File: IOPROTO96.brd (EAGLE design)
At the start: 38.1 x 39.4 mm, 4 parts

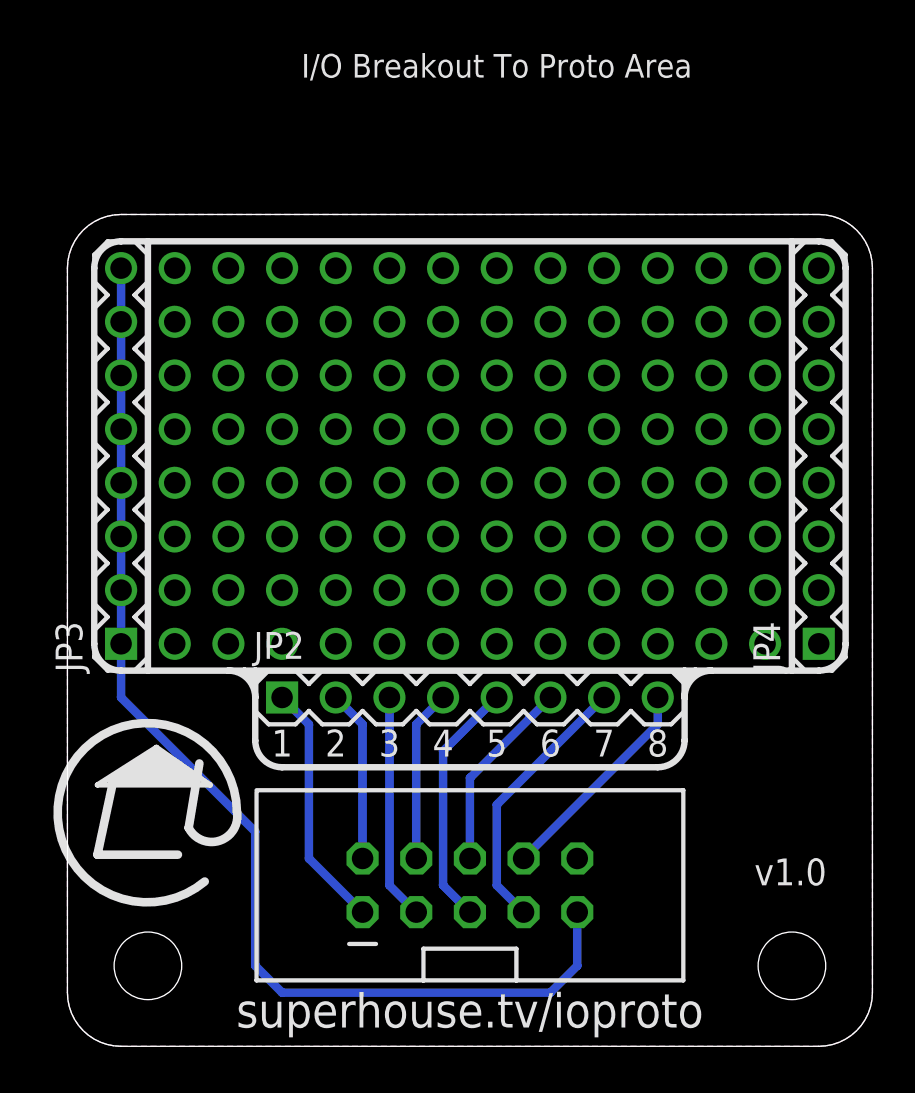
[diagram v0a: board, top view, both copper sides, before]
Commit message: Updated silkscreen for v2.0 release
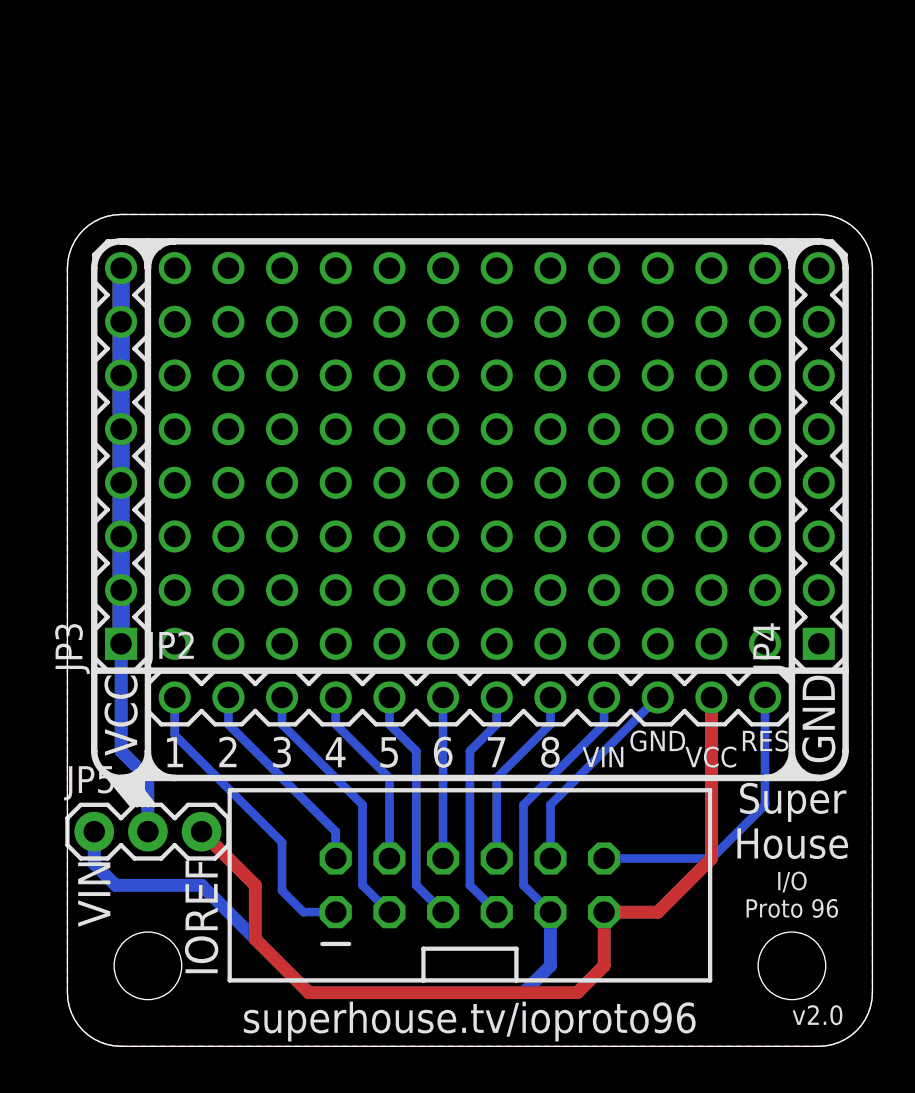
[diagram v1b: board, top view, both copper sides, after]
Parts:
- added JP5: (no value), freetronics-jon:1X03
- JP1: value M05X2SHD -> M06X2; device freetronics-original:2X5-SHROUDED -> freetronics-jon:2X6-SHROUDED
- JP2: value (none) -> M12PTH; device freetronics-master-v1:1X08 -> freetronics-original:1X12
- moved JP1 6.48 mm to (12.7, 6.35)
- moved JP2 5.08 mm to (5.08, 16.5)
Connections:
- net N$11 renamed D5
- net N$12 renamed D3
- net N$13 renamed D1
- net N$14 renamed D7
- net N$27 renamed D8
- net N$28 renamed D6
- net N$29 renamed D4
- net N$30 renamed D2
- removed net VCC: JP1.9, JP3.1, JP3.2, JP3.3, JP3.4, JP3.5, JP3.6, JP3.7, JP3.8
- new net IOREF: JP1.11, JP2.11, JP5.3
- new net RESET: JP1.12, JP2.12
- new net V+: JP3.1, JP3.2, JP3.3, JP3.4, JP3.5, JP3.6, JP3.7, JP3.8, JP5.2
- new net VIN: JP1.9, JP2.9, JP5.1
- net GND: now also JP2.10
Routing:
- net VCC: track 54.5 -> 0.00 mm
- net VIN: track 0.00 -> 41.0 mm
- net IOREF: track 0.00 -> 40.5 mm
- net V+: track 0.00 -> 27.2 mm
- net RESET: track 0.00 -> 13.8 mm
- net GND: track 0.00 -> 9.72 mm
- net D1: track 11.7 -> 14.2 mm
- net D8: track 10.3 -> 8.67 mm
- net D3: track 10.7 -> 12.3 mm
- net D6: track 9.20 -> 7.62 mm
- net D2: track 8.15 -> 9.72 mm
- net D7: track 12.8 -> 11.2 mm
- net D4: track 8.15 -> 8.67 mm
- net D5: track 11.7 -> 11.2 mm
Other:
- board text added: "(c) 2017 SuperHouse"
- board text added: "I/O Proto 96"
- board text added: "IOREF"
- board text added: "RES"
- board text added: "RESET"
- board text added: "SKU: IOPROTO96"
- board text added: "Super House"
- board text added: "VIN"
- board text added: "superhouse.tv/ioproto96"
- board text added: "v2.0"
- board text removed: "(c) 2017 SuperHouse Pty Ltd"
- board text removed: "I/O Breakout To Proto Area"
- board text removed: "Licensed under the TAPR"
- board text removed: "Open Hardware License"
- board text removed: "SKU: IOTERM"
- board text removed: "superhouse.tv/ioproto"
- board text removed: "v1.0"
- board text removed: "www.tapr.org/OHL"

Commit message: Final routing and DRC for release v2.0
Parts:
- moved JP5 4.58 mm to (3.81, 6.35), turned to 90 degrees
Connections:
- net D1 renamed IO1
- net D2 renamed IO2
- net D3 renamed IO3
- net D4 renamed IO4
- net D5 renamed IO5
- net D6 renamed IO6
- net D7 renamed IO7
- net D8 renamed IO8
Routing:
- net GND: track 9.72 -> 0.00 mm
- net VIN: track 41.0 -> 36.0 mm
- net IOREF: track 40.5 -> 44.3 mm
- net V+: track 27.2 -> 30.3 mm
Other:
- board text added: "IO REF"

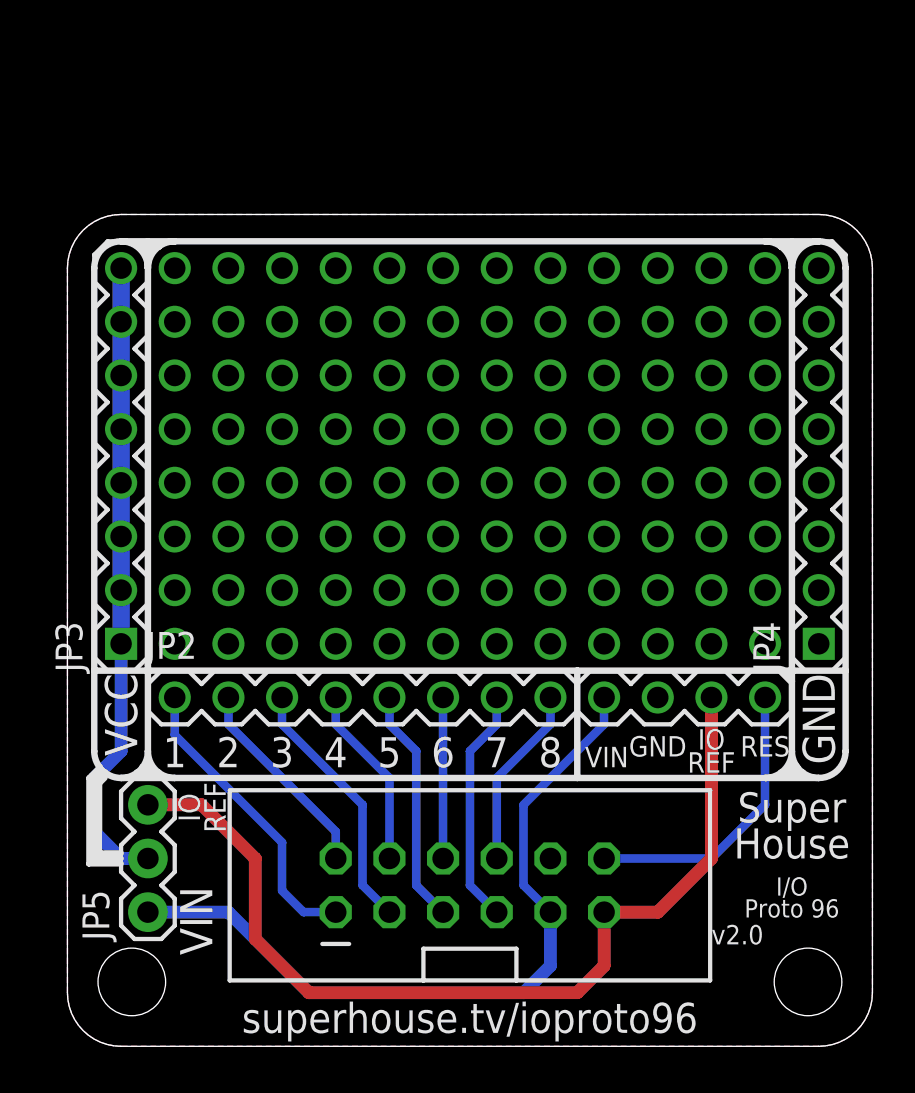
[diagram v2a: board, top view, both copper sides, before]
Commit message: Part replacement using SuperHouse libraries
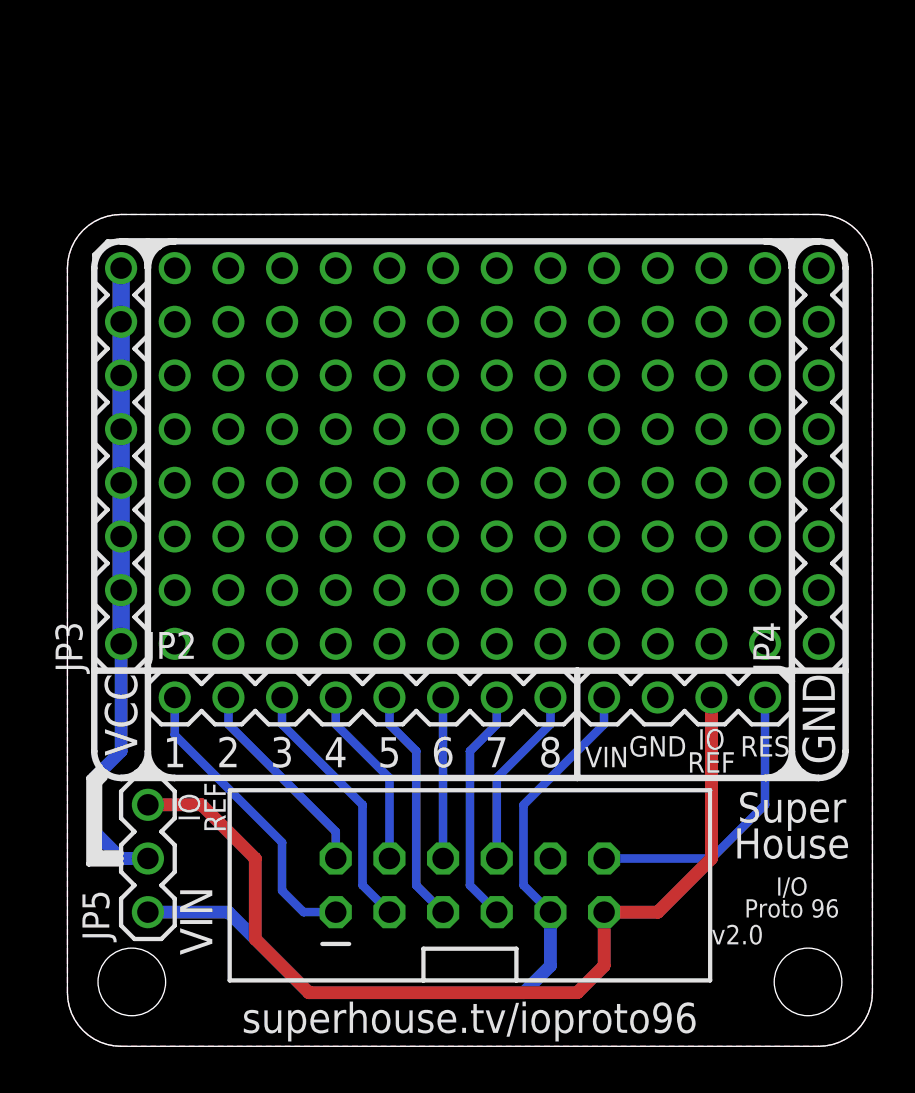
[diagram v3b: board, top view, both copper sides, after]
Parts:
- JP1: value M06X2 -> M06X2-SHROUDED; device freetronics-jon:2X6-SHROUDED -> SuperHouse-Connectors:2X6-SHROUDED
- JP2: value M12PTH -> M12-PLAIN; device freetronics-original:1X12 -> SuperHouse-Connectors:1X12
- JP3, JP4: value (none) -> M08-PLAIN; device freetronics-master-v1:1X08 -> SuperHouse-Connectors:1X08
- JP5: device freetronics-jon:1X03 -> SuperHouse-Connectors:1X03-P
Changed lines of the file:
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@@
 <?xml version="1.0" encoding="utf-8"?>
 <!DOCTYPE eagle SYSTEM "eagle.dtd">
-<eagle version="6.5.0">
+<eagle version="9.4.2">
 <drawing>
 <settings>
 <setting alwaysvectorfont="yes"/>
+<setting keepoldvectorfont="yes"/>
 <setting verticaltext="up"/>
 </settings>
@@
 <layer number="60" name="bCarbon" color="7" fill="1" visible="no" active="no"/>
 <layer number="61" name="pt_docu" color="7" fill="0" visible="no" active="no"/>
-<layer number="90" name="Modules" color="7" fill="1" visible="yes" active="yes"/>
+<layer number="88" name="SimResults" color="9" fill="1" visible="no" active="no"/>
+<layer number="89" name="SimProbes" color="9" fill="1" visible="no" active="no"/>
+<layer number="90" name="Modules" color="7" fill="1" visible="no" active="no"/>
 <layer number="91" name="Nets" color="2" fill="1" visible="no" active="no"/>
 <layer number="92" name="Busses" color="1" fill="1" visible="no" active="no"/>
@@
 <layer number="131" name="tAdjust" color="7" fill="1" visible="yes" active="yes"/>
 <layer number="132" name="bAdjust" color="7" fill="1" visible="yes" active="yes"/>
+<layer number="133" name="bottom_silk" color="7" fill="1" visible="yes" active="yes"/>
+<layer number="134" name="silk_top" color="7" fill="1" visible="no" active="no"/>
+<layer number="135" name="silk_bottom" color="7" fill="1" visible="no" active="no"/>
+<layer number="136" name="silktop" color="7" fill="1" visible="yes" active="yes"/>
+<layer number="137" name="silkbottom" color="7" fill="1" visible="yes" active="yes"/>
+<layer number="138" name="GND@2" color="7" fill="1" visible="yes" active="yes"/>
+<layer number="139" name="mtKeepout" color="7" fill="1" visible="yes" active="yes"/>
+<layer number="140" name="mbKeepout" color="7" fill="1" visible="yes" active="yes"/>
+<layer number="141" name="mtRestrict" color="7" fill="1" visible="yes" active="yes"/>
+<layer number="142" name="mbRestrict" color="7" fill="1" visible="yes" active="yes"/>
+<layer number="143" name="mvRestrict" color="7" fill="1" visible="yes" active="yes"/>
 <layer number="144" name="Drill_legend" color="7" fill="1" visible="yes" active="yes"/>
+<layer number="145" name="DrillLegend_01-16" color="7" fill="1" visible="yes" active="yes"/>
 <layer number="146" name="p_Milling" color="3" fill="9" visible="no" active="yes"/>
 <layer number="147" name="COVER" color="14" fill="1" visible="no" active="yes"/>
+<layer number="148" name="mDocument" color="7" fill="1" visible="yes" active="yes"/>
+<layer number="149" name="mReference" color="7" fill="1" visible="yes" active="yes"/>
 <layer number="150" name="Notes" color="7" fill="1" visible="yes" active="yes"/>
 <layer number="151" name="HeatSink" color="7" fill="1" visible="yes" active="yes"/>
@@
 <layer number="154" name="FabDoc2" color="2" fill="1" visible="no" active="no"/>
 <layer number="155" name="FabDoc3" color="7" fill="15" visible="no" active="no"/>
+<layer number="166" name="AntennaArea" color="7" fill="1" visible="yes" active="yes"/>
+<layer number="168" name="4mmHeightArea" color="7" fill="1" visible="yes" active="yes"/>
 <layer number="190" name="Comments" color="12" fill="1" visible="no" active="yes"/>
+<layer number="191" name="mNets" color="7" fill="1" visible="yes" active="yes"/>
+<layer number="192" name="mBusses" color="7" fill="1" visible="yes" active="yes"/>
+<layer number="193" name="mPins" color="7" fill="1" visible="yes" active="yes"/>
+<layer number="194" name="mSymbols" color="7" fill="1" visible="yes" active="yes"/>
+<layer number="195" name="mNames" color="7" fill="1" visible="yes" active="yes"/>
+<layer number="196" name="mValues" color="7" fill="1" visible="yes" active="yes"/>
 <layer number="199" name="Contour" color="7" fill="1" visible="yes" active="yes"/>
 <layer number="200" name="200bmp" color="1" fill="10" visible="no" active="no"/>
@@
 </layers>
 <board>
+<fusionsync huburn="a.cGVyc29uYWw6dWUyZDliZmNi" projecturn="a.cGVyc29uYWw6dWUyZDliZmNiIzIwMTkwNjE5MTk5NjgzNjgx" f3durn="urn:adsk.wipprod:dm.lineage:sJhRnrLATc-Ulerov-CTvA" pcbguid="8905ec94-9653-4335-8bae-5ca6b5da45ba" lastpulledtime="" lastsyncedchangeguid="452cceca-822e-6409-229e-01c5fc7548fb"/>
 <plain>
 <text x="21.082" y="13.462" size="1.016" layer="22" font="vector" ratio="16" rot="SMR0">(c) 2017 SuperHouse</text>
@@
 <param name="dpMaxLengthDifference" value="10mm"/>
 <param name="dpGapFactor" value="2.5"/>
-<param name="checkGrid" value="0"/>
 <param name="checkAngle" value="0"/>
 <param name="checkFont" value="1"/>
 <param name="checkRestrict" value="1"/>
+<param name="checkStop" value="0"/>
+<param name="checkValues" value="0"/>
+<param name="checkNames" value="1"/>
+<param name="checkWireStubs" value="1"/>
+<param name="checkPolygonWidth" value="0"/>
 <param name="useDiameter" value="13"/>
 <param name="maxErrors" value="50"/>
@@
 <pass name="Default">
 <param name="RoutingGrid" value="50mil"/>
+<param name="AutoGrid" value="1"/>
+<param name="Efforts" value="0"/>
+<param name="TopRouterVariant" value="1"/>
 <param name="tpViaShape" value="round"/>
 <param name="PrefDir.1" value="|"/>
@@
 </autorouter>
 <elements>
-<element name="JP1" library="freetronics-jon" package="2X6-SHROUDED" value="M06X2" x="12.7" y="6.35" rot="R90"/>
-<element name="JP2" library="freetronics-original" package="1X12" value="M12PTH" x="5.08" y="16.51"/>
-<element name="JP3" library="freetronics-master-v1" package="1X08" value="" x="2.54" y="19.05" rot="R90"/>
-<element name="JP4" library="freetronics-master-v1" package="1X08" value="" x="35.56" y="19.05" rot="R90"/>
-<element name="JP5" library="freetronics-jon" package="1X03" value="" x="3.81" y="6.35" rot="R90"/>
+<element name="JP1" library="SuperHouse-Connectors" library_urn="urn:adsk.eagle:library:11765989" package="2X6-SHROUDED" package3d_urn="urn:adsk.eagle:package:11976015/2" value="M06X2-SHROUDED" x="12.7" y="6.35" smashed="yes" rot="R90">
+<attribute name="NAME" x="31.242" y="4.699" size="0.4064" layer="104" rot="R90"/>
+<attribute name="VALUE" x="7.366" y="4.699" size="0.4064" layer="27" font="vector" rot="R90"/>
+</element>
+<element name="JP2" library="SuperHouse-Connectors" library_urn="urn:adsk.eagle:library:11765989" package="1X12" package3d_urn="urn:adsk.eagle:package:12194678/1" value="M12-PLAIN" x="5.08" y="16.51" smashed="yes">
+<attribute name="NAME" x="3.7338" y="18.3388" size="1.27" layer="25" ratio="10"/>
+<attribute name="VALUE" x="3.81" y="13.335" size="1.27" layer="27"/>
+</element>
+<element name="JP3" library="SuperHouse-Connectors" library_urn="urn:adsk.eagle:library:11765989" package="1X08" package3d_urn="urn:adsk.eagle:package:11866882/1" value="M08-PLAIN" x="2.54" y="19.05" smashed="yes" rot="R90">
+<attribute name="NAME" x="0.7112" y="17.7038" size="1.27" layer="25" ratio="10" rot="R90"/>
+<attribute name="VALUE" x="5.715" y="17.78" size="1.27" layer="27" rot="R90"/>
+</element>
+<element name="JP4" library="SuperHouse-Connectors" library_urn="urn:adsk.eagle:library:11765989" package="1X08" package3d_urn="urn:adsk.eagle:package:11866882/1" value="M08-PLAIN" x="35.56" y="19.05" smashed="yes" rot="R90">
+<attribute name="NAME" x="33.7312" y="17.7038" size="1.27" layer="25" ratio="10" rot="R90"/>
+<attribute name="VALUE" x="38.735" y="17.78" size="1.27" layer="27" rot="R90"/>
+</element>
+<element name="JP5" library="SuperHouse-Connectors" library_urn="urn:adsk.eagle:library:11765989" package="1X03-P" package3d_urn="urn:adsk.eagle:package:11815967/3" value="" x="3.81" y="6.35" smashed="yes" rot="R90">
+<attribute name="NAME" x="1.9812" y="5.0038" size="1.27" layer="25" ratio="10" rot="R90"/>
+<attribute name="VALUE" x="6.985" y="5.08" size="1.27" layer="27" rot="R90"/>
+</element>
 </elements>
 <signals>
@@
 </signal>
 </signals>
+<mfgpreviewcolors>
+<mfgpreviewcolor name="soldermaskcolor" color="0xC8008000"/>
+<mfgpreviewcolor name="silkscreencolor" color="0xFFFEFEFE"/>
+<mfgpreviewcolor name="backgroundcolor" color="0xFF282828"/>
+<mfgpreviewcolor name="coppercolor" color="0xFFFFBF00"/>
+<mfgpreviewcolor name="substratecolor" color="0xFF786E46"/>
+</mfgpreviewcolors>
 <errors>
 </errors>
@@
 which will not be processed correctly with this version.
 </note>
+<note version="8.2" severity="warning">
+Since Version 8.2, EAGLE supports online libraries. The ids
+of those online libraries will not be understood (or retained)
+with this version.
+</note>
+<note version="8.3" severity="warning">
+Since Version 8.3, EAGLE supports Fusion synchronisation.
+This feature will not be available in this version and saving
+the document will break the link to the Fusion PCB feature.
+</note>
+<note version="8.3" severity="warning">
+Since Version 8.3, EAGLE supports URNs for individual library
+assets (packages, symbols, and devices). The URNs of those assets
+will not be understood (or retained) with this version.
+</note>
+<note version="8.3" severity="warning">
+Since Version 8.3, EAGLE supports the association of 3D packages
+with devices in libraries, schematics, and board files. Those 3D
+packages will not be understood (or retained) with this version.
+</note>
 </compatibility>
